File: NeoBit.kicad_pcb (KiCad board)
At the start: 2 copper layers, 77.5 x 45.7 mm, 22 parts, among them J1 AudioJack3_Ground, J2 Barrel_Jack_MountingPin, J3 Qwiic, J4 DotStars, J5 microbit_edge_connector, J6 NeoPixels, U1 74AHCT125, U2 MCP1702-3302E_TO92, U3 MCP1702-5002E_TO92

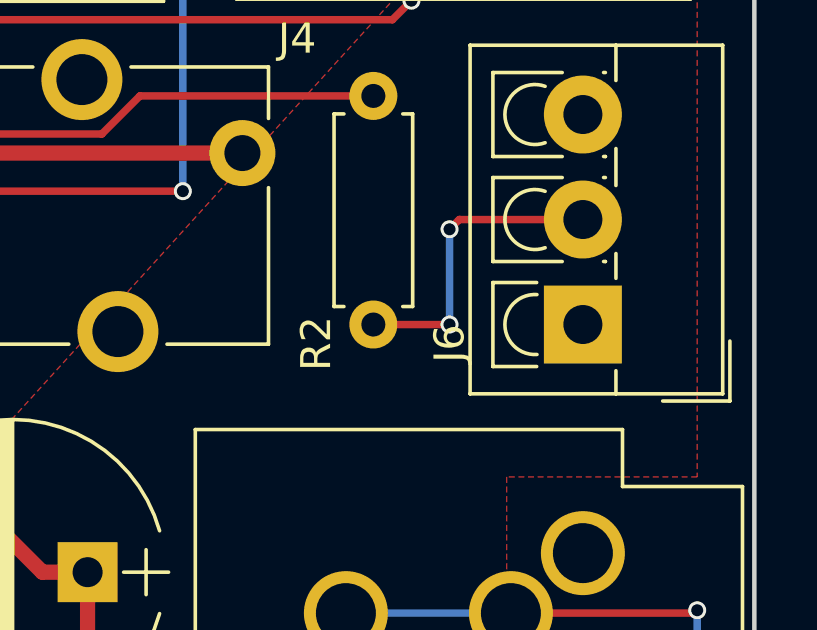
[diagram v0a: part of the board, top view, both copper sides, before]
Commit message: Finish adding silkscreen.
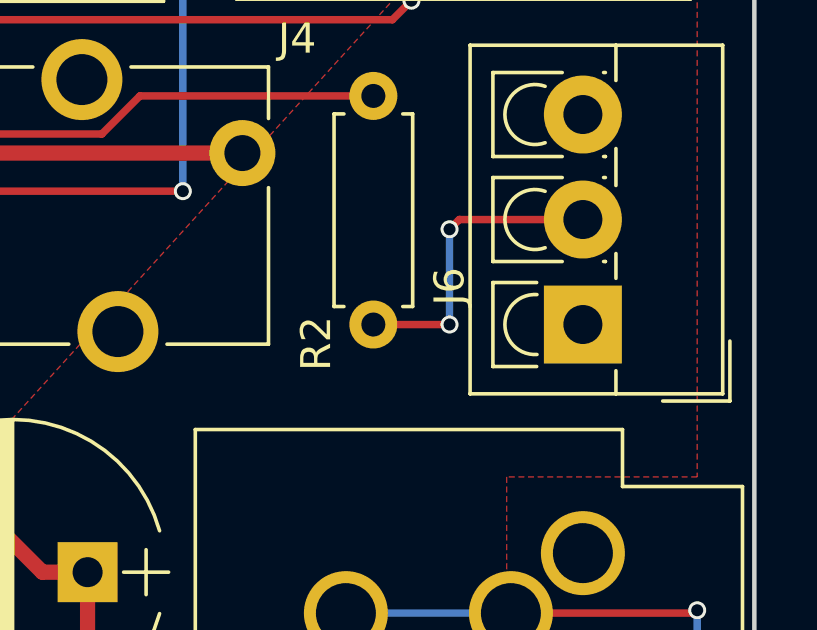
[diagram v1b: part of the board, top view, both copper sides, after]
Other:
- board text added: "CLK"
- board text added: "DAT"
- board text added: "DotStars"
- board text added: "QWIIC"
- board text added: "headphones"
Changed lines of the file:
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@@
     (area 118.669999 83.744999 186.130001 129.615001)
     (thickness 1.6)
-    (drawings 14)
+    (drawings 21)
     (tracks 194)
     (zones 0)
@@
     (descr "Terminal Block 4Ucon ItemNo. 10694, vertical (cable from top), 3 pins, pitch 3.5mm, size 11.5x8.3mm^2, drill diamater 1.3mm, pad diameter 2.6mm, see http://www.4uconnector.com/online/object/4udrawing/10694.pdf, script-generated with , script-generated using https://github.com/pointhi/kicad-footprint-generator/scripts/TerminalBlock_4Ucon")
     (tags "THT Terminal Block 4Ucon ItemNo. 10694 vertical pitch 3.5mm size 11.5x8.3mm^2 drill 1.3mm pad 2.6mm")
-    (fp_text reference J6 (at -0.635 -4.445 90) (layer F.SilkS)
+    (fp_text reference J6 (at 1.27 -4.445 90) (layer F.SilkS)
       (effects (font (size 1 1) (thickness 0.15)))
     )
@@
     )
   )
+  (gr_text QWIIC (at 120.65 109.855 270) (layer B.SilkS)
+    (effects (font (size 1 1) (thickness 0.2)) (justify mirror))
+  )
+  (gr_text DotStars (at 186.69 91.44) (layer B.SilkS)
+    (effects (font (size 1 1) (thickness 0.2)) (justify mirror))
+  )
+  (gr_text GND (at 181.356 87.376 90) (layer B.SilkS)
+    (effects (font (size 1 1) (thickness 0.2)) (justify right mirror))
+  )
+  (gr_text DAT (at 184.912 87.376 90) (layer B.SilkS)
+    (effects (font (size 1 1) (thickness 0.2)) (justify right mirror))
+  )
+  (gr_text CLK (at 188.468 87.376 90) (layer B.SilkS)
+    (effects (font (size 1 1) (thickness 0.2)) (justify right mirror))
+  )
+  (gr_text +V (at 191.77 87.376 90) (layer B.SilkS)
+    (effects (font (size 1 1) (thickness 0.2)) (justify right mirror))
+  )
+  (gr_text headphones (at 194.945 111.76 90) (layer B.SilkS)
+    (effects (font (size 1 1) (thickness 0.2)) (justify mirror))
+  )
   (gr_line (start 121.285 129.54) (end 193.675 129.54) (angle 90) (layer Edge.Cuts) (width 0.15))

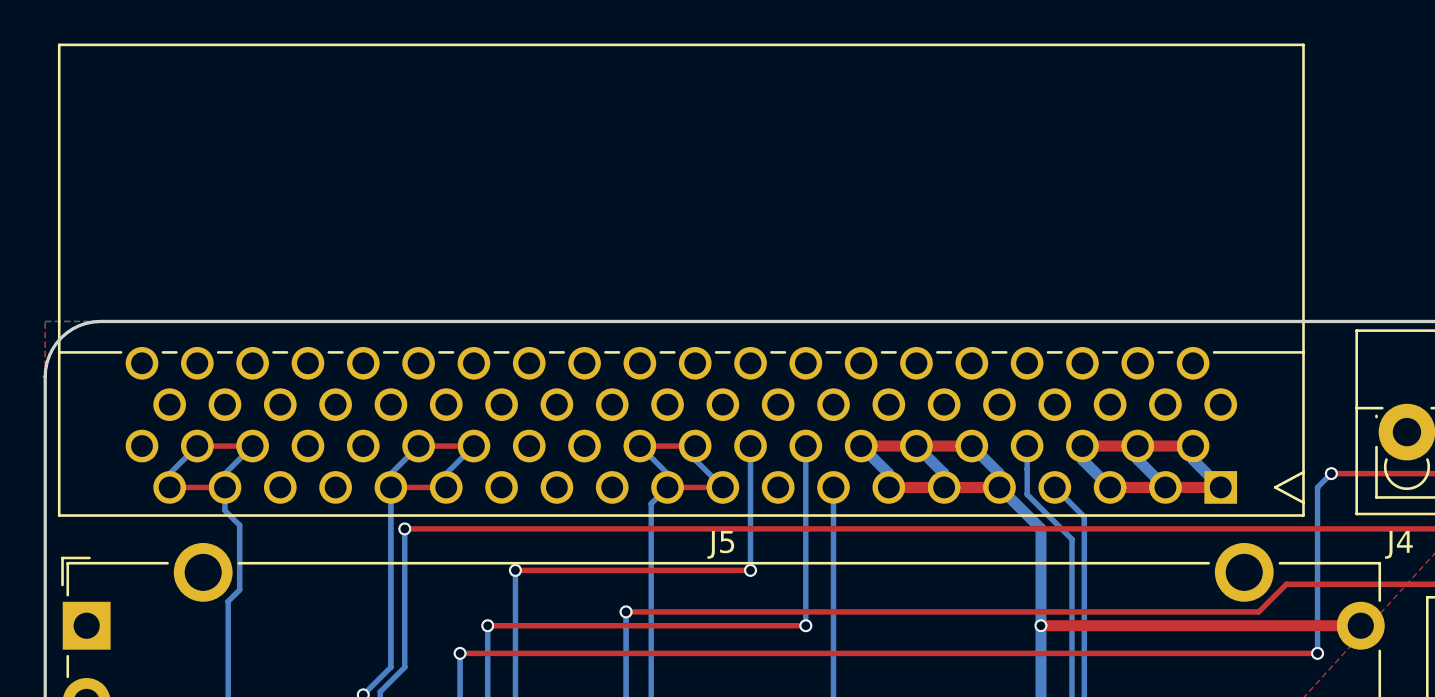
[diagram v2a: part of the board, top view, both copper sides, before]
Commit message: Use new footprint for micro:bit edge connector.
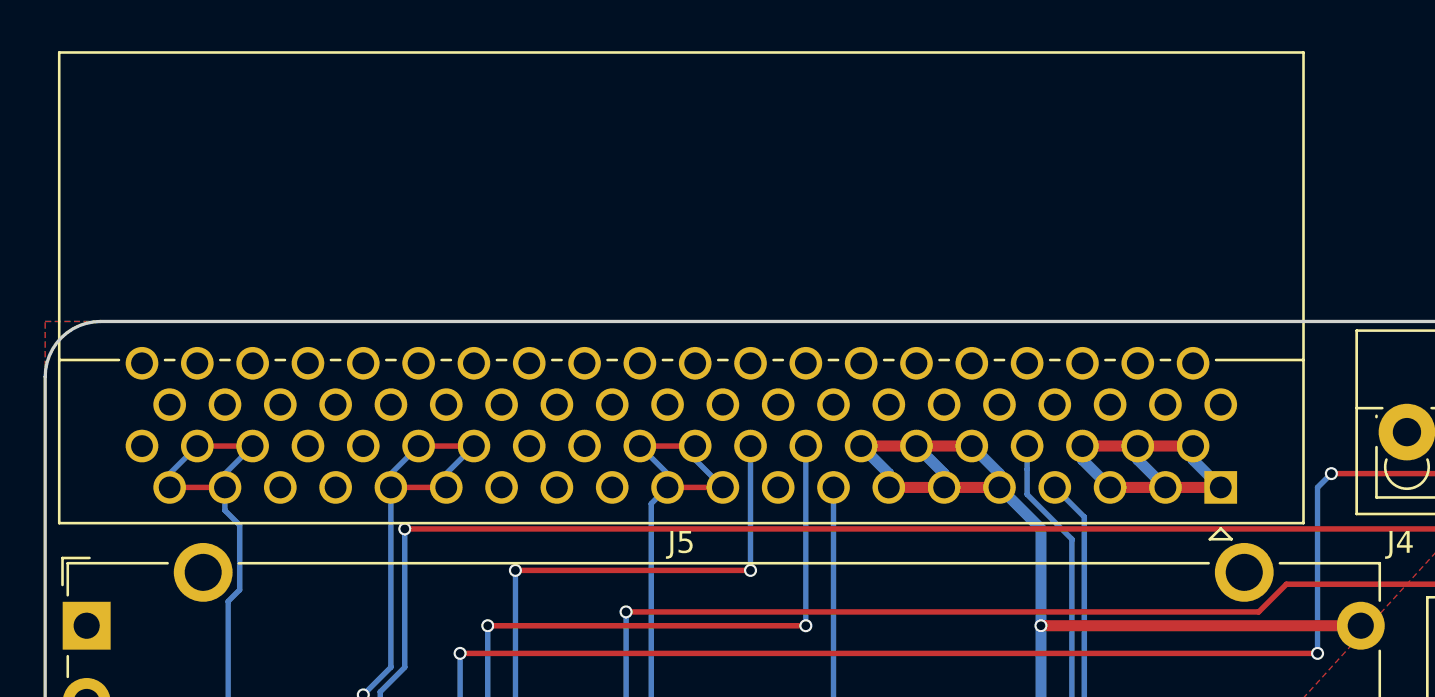
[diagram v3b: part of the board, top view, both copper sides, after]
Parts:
- J5: footprint footprints:4UCON_10156_90deg -> footprints:4UCON_10156_2x40_P1.27mm_Socket_Horizontal

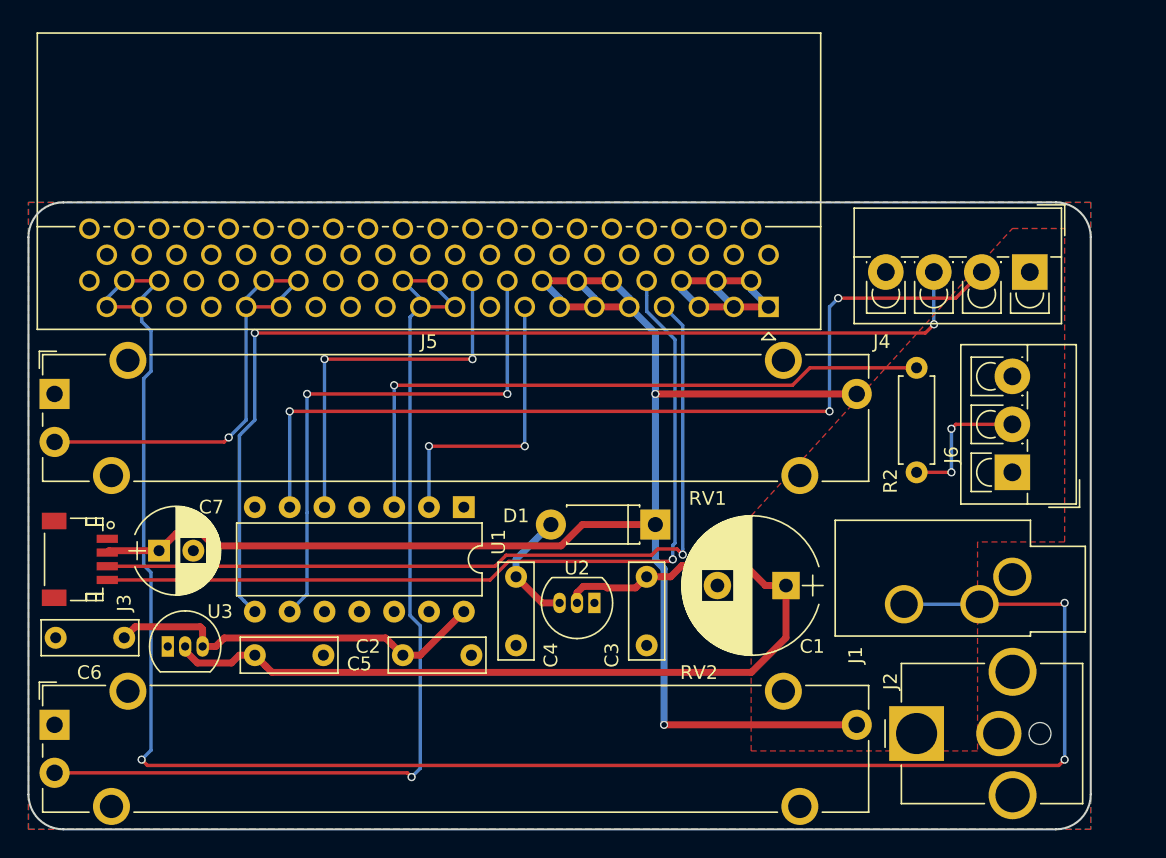
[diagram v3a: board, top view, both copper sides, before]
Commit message: Cram audio filter into PCB.
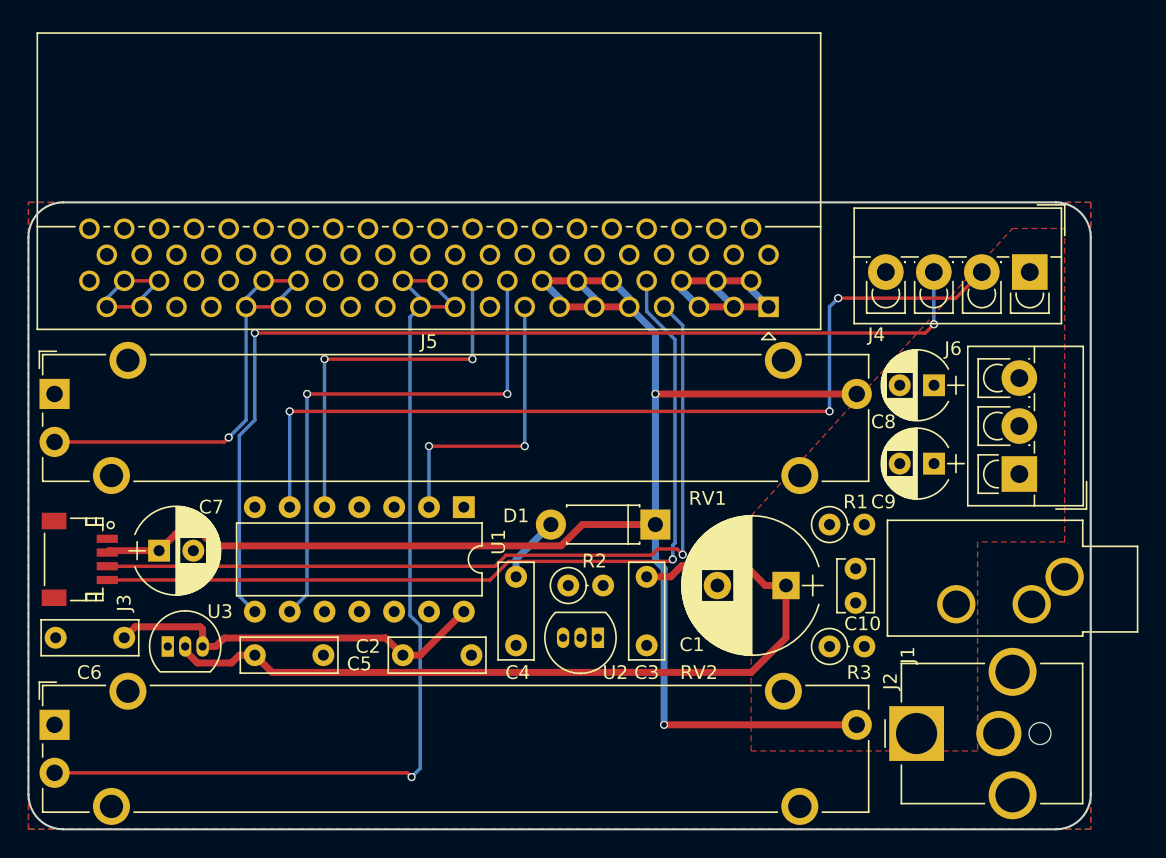
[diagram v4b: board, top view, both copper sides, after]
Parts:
- added C10: 10nF, Capacitors_THT:C_Disc_D3.8mm_W2.6mm_P2.50mm, F.Cu at (179.1, 113.0)
- added C8: 220uF, Capacitors_THT:CP_Radial_D5.0mm_P2.50mm, F.Cu at (184.8, 97.2)
- added C9: 220uF, Capacitors_THT:CP_Radial_D5.0mm_P2.50mm, F.Cu at (184.8, 102.9)
- added R1: 100, Resistors_THT:R_Axial_DIN0207_L6.3mm_D2.5mm_P2.54mm_Vertical, F.Cu at (177.2, 107.3)
- added R3: 22, Resistors_THT:R_Axial_DIN0207_L6.3mm_D2.5mm_P2.54mm_Vertical, F.Cu at (177.2, 116.2)
- R2: footprint Resistors_THT:R_Axial_DIN0207_L6.3mm_D2.5mm_P7.62mm_Horizontal -> Resistors_THT:R_Axial_DIN0207_L6.3mm_D2.5mm_P2.54mm_Vertical
- moved R2 30.0 mm to (158.1, 111.8), turned to 0 degrees
- moved G*** 4.26 mm to (161.3, 123.8)
- moved J1 3.81 mm to (194.3, 111.1)
- moved U2 2.55 mm to (160.3, 115.6)
- moved REF*** 2.29 mm to (141.0, 123.8)
- moved J6 0.52 mm to (191.0, 103.6)
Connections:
- J1 pad R: /P0 -> Net-(C9-Pad1)
- J1 pad T: /P0 -> Net-(C8-Pad1)
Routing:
- net /P0: track 134.8 -> 9.93 mm, vias 3 -> 0
- net Net-(R2-Pad1): track 47.5 -> 0.00 mm, vias 1 -> 0
- net Net-(J6-Pad2): track 10.3 -> 0.00 mm, vias 2 -> 0
- net +VDC: track 67.6 -> 61.2 mm
- net Net-(C4-Pad1): track 8.83 -> 4.86 mm
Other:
- board text added: "2018-09-23 https://github.com/ppelleti/NeoBit designed by Patrick Pelletier"
- board text removed: "2018-09-22 https://github.com/ppelleti/NeoBit designed by Patrick Pelletier"

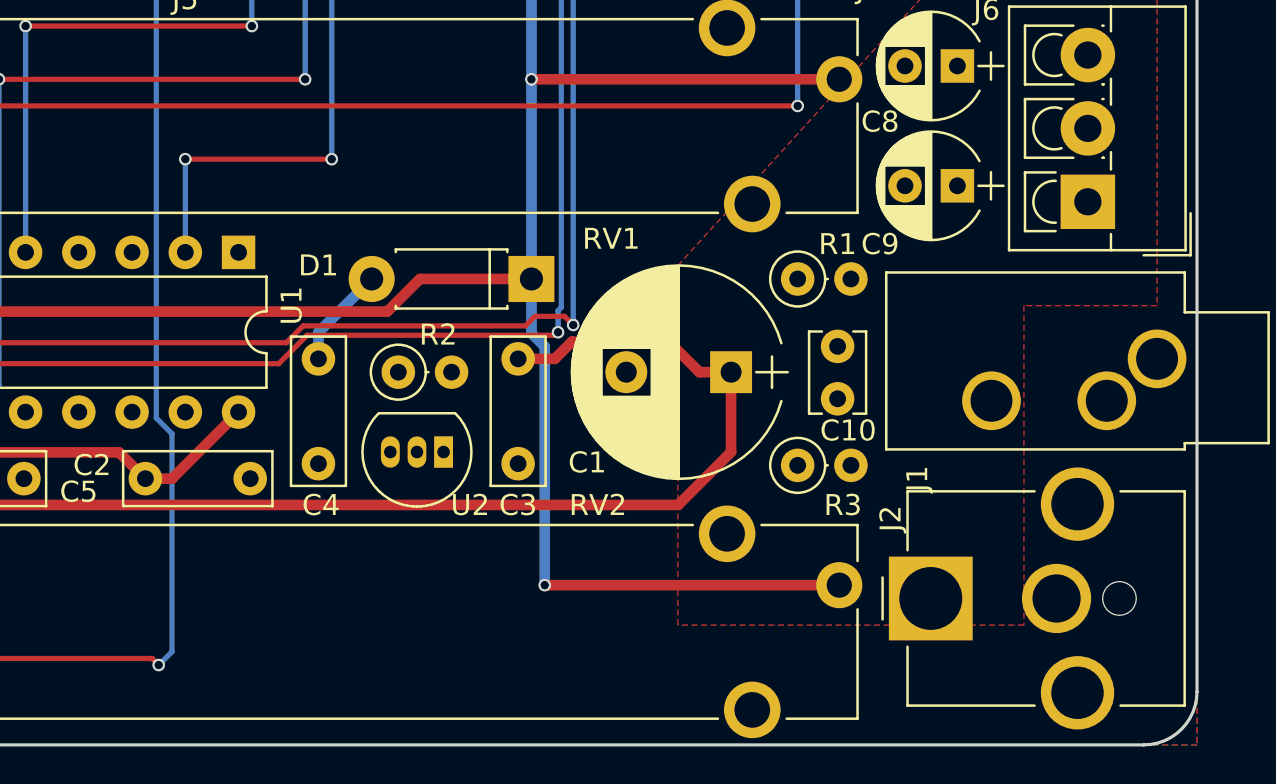
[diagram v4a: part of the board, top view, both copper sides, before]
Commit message: Draw a few tracks.
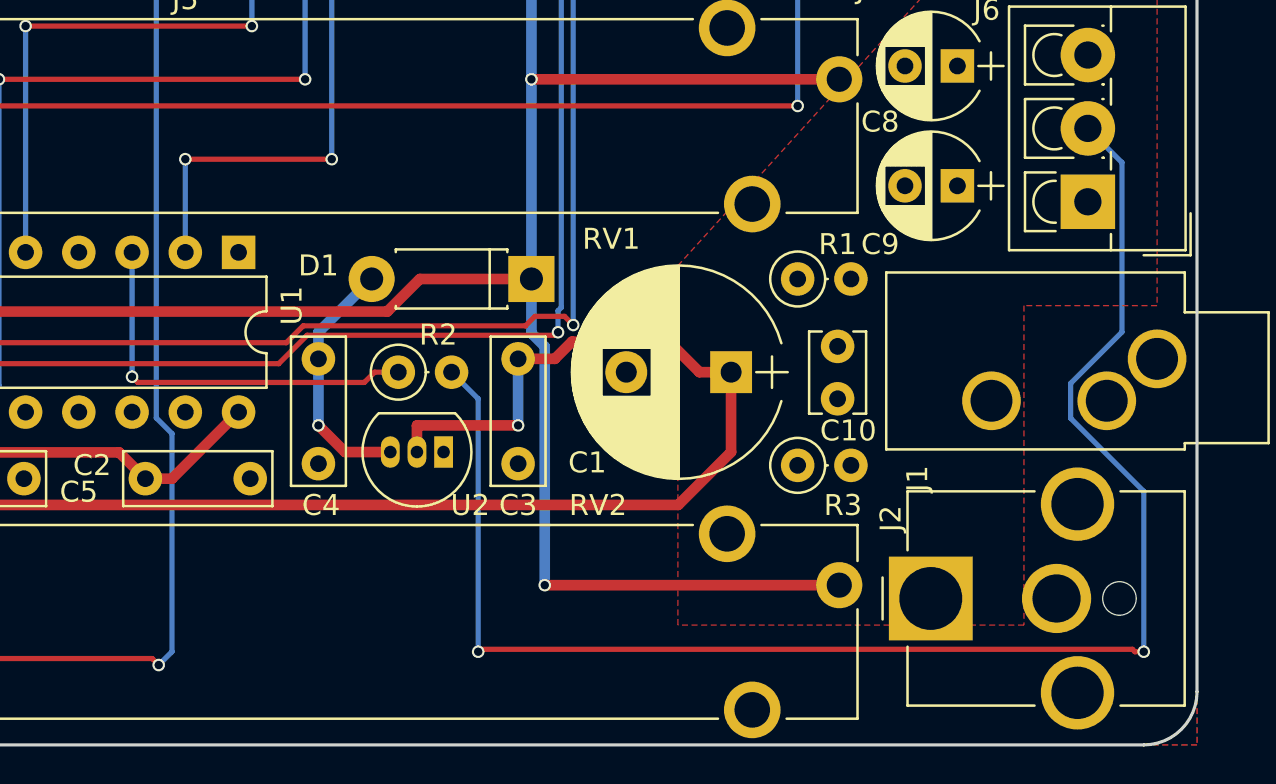
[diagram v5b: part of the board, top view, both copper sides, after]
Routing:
- net Net-(J6-Pad2): track 0.00 -> 73.8 mm, vias 0 -> 2
- net Net-(R2-Pad1): track 0.00 -> 18.9 mm, vias 0 -> 1
- net +VDC: track 61.2 -> 70.5 mm, vias 0 -> 1
- net Net-(C4-Pad1): track 4.86 -> 12.0 mm, vias 0 -> 1
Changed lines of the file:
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@@
     (thickness 1.6)
     (drawings 21)
-    (tracks 149)
+    (tracks 178)
     (zones 0)
     (modules 27)
@@
   (segment (start 166.37 89.54) (end 166.37 90.17) (width 0.508) (layer B.Cu) (net 2) (status 30))
   (segment (start 166.37 90.17) (end 167.64 91.44) (width 0.508) (layer B.Cu) (net 2) (status 30))
+  (segment (start 154.305 114.3) (end 154.305 111.125) (width 0.508) (layer B.Cu) (net 3))
+  (segment (start 157.734 115.57) (end 155.575 115.57) (width 0.508) (layer F.Cu) (net 3))
+  (segment (start 155.575 115.57) (end 154.305 114.3) (width 0.508) (layer F.Cu) (net 3))
+  (via (at 154.305 114.3) (size 0.6) (drill 0.4) (layers F.Cu B.Cu) (net 3))
   (segment (start 154.305 111.125) (end 154.305 109.855) (width 0.508) (layer B.Cu) (net 3) (status 10))
   (segment (start 154.305 109.855) (end 156.845 107.315) (width 0.508) (layer B.Cu) (net 3) (status 20))
@@
   (segment (start 146.375 125.42) (end 146.685 125.73) (width 0.25) (layer F.Cu) (net 7))
   (via (at 146.685 125.73) (size 0.6) (drill 0.4) (layers F.Cu B.Cu) (net 7))
+  (segment (start 145.415 111.98) (end 145.415 106.045) (width 0.25) (layer B.Cu) (net 8))
+  (segment (start 158.115 111.76) (end 156.98363 111.76) (width 0.25) (layer F.Cu) (net 8))
+  (segment (start 156.98363 111.76) (end 156.493629 112.250001) (width 0.25) (layer F.Cu) (net 8))
+  (via (at 145.415 111.98) (size 0.6) (drill 0.4) (layers F.Cu B.Cu) (net 8))
+  (segment (start 156.493629 112.250001) (end 145.685001 112.250001) (width 0.25) (layer F.Cu) (net 8))
+  (segment (start 145.685001 112.250001) (end 145.415 111.98) (width 0.25) (layer F.Cu) (net 8))
+  (segment (start 163.83 114.3) (end 159.016 114.3) (width 0.508) (layer F.Cu) (net 9))
+  (segment (start 159.016 114.3) (end 159.004 114.312) (width 0.508) (layer F.Cu) (net 9))
+  (segment (start 159.004 114.312) (end 159.004 115.57) (width 0.508) (layer F.Cu) (net 9))
+  (segment (start 163.83 111.125) (end 163.83 114.3) (width 0.508) (layer B.Cu) (net 9))
+  (via (at 163.83 114.3) (size 0.6) (drill 0.4) (layers F.Cu B.Cu) (net 9))
   (segment (start 165.580924 111.125) (end 163.83 111.125) (width 0.508) (layer F.Cu) (net 9) (status 20))
   (segment (start 172.482 111.76) (end 171.027999 110.305999) (width 0.508) (layer F.Cu) (net 9))
@@
   (segment (start 147.955 106.045) (end 147.955 101.6) (width 0.25) (layer B.Cu) (net 14) (status 10))
   (via (at 147.955 101.6) (size 0.6) (drill 0.4) (layers F.Cu B.Cu) (net 14))
+  (segment (start 161.925 125.095) (end 161.925 113.03) (width 0.25) (layer B.Cu) (net 15))
+  (segment (start 161.925 113.03) (end 160.655 111.76) (width 0.25) (layer B.Cu) (net 15))
+  (segment (start 193.675 125.095) (end 193.250736 125.095) (width 0.25) (layer F.Cu) (net 15))
+  (segment (start 193.250736 125.095) (end 193.135735 124.979999) (width 0.25) (layer F.Cu) (net 15))
+  (segment (start 162.040001 124.979999) (end 161.925 125.095) (width 0.25) (layer F.Cu) (net 15))
+  (segment (start 193.135735 124.979999) (end 162.040001 124.979999) (width 0.25) (layer F.Cu) (net 15))
+  (via (at 161.925 125.095) (size 0.6) (drill 0.4) (layers F.Cu B.Cu) (net 15))
+  (segment (start 191.008 100.132) (end 192.633001 101.757001) (width 0.25) (layer B.Cu) (net 15))
+  (segment (start 192.633001 101.757001) (end 192.633001 109.848997) (width 0.25) (layer B.Cu) (net 15))
+  (segment (start 192.633001 109.848997) (end 190.184999 112.296999) (width 0.25) (layer B.Cu) (net 15))
+  (segment (start 190.184999 112.296999) (end 190.184999 113.953001) (width 0.25) (layer B.Cu) (net 15))
+  (segment (start 190.184999 113.953001) (end 193.675 117.443002) (width 0.25) (layer B.Cu) (net 15))
+  (segment (start 193.675 117.443002) (end 193.675 125.095) (width 0.25) (layer B.Cu) (net 15))
+  (via (at 193.675 125.095) (size 0.6) (drill 0.4) (layers F.Cu B.Cu) (net 15))
   (segment (start 137.795 99.06) (end 137.795 106.045) (width 0.25) (layer B.Cu) (net 16) (status 20))
   (segment (start 177.165 99.06) (end 137.795 99.06) (width 0.25) (layer F.Cu) (net 16))
